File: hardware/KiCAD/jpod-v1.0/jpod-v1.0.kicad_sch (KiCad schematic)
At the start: 47 parts, among them J1 SD_Card, J2 SPI_DEBUG, J3 LCD_HEADER, J4 3.5mm Jack, Q1 AO3400A, U1 ESP32, U2 1.8V Regulator, U3 DAC, U4 Charger, U5 Buck Boost, U6 Fuel Gauge

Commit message: battery updates and switch added to library:
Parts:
- added S1: JS102011SAQN, JS102011SAQN:SW_JS102011SAQN, symbol jpod:JS102011SAQN
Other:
- note added: "These are for the AVDD/DVDD... power on DAC However they are identical. Maybe a cleaner way to display this?"
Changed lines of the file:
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@@
+    (effects (font (size 1.27 1.27)) (justify left bottom))
+  )
+  (text "These are for the AVDD/DVDD... power on DAC\nHowever they are identical. Maybe a cleaner way to display this?\n"
+    (at 18.288 159.512 0)
     (effects (font (size 1.27 1.27)) (justify left bottom))
   )
@@
         )
       )
+    )
+  )
+  (symbol (lib_id "jpod:JS102011SAQN") (at 519.049 279.781 0) (unit 1)
+    (in_bom yes) (on_board yes) (dnp no) (fields_autoplaced)
+    (property "Reference" "S1" (at 519.049 271.78 0)
+      (effects (font (size 1.27 1.27)))
+    )
+    (property "Value" "JS102011SAQN" (at 519.049 274.32 0)
+      (effects (font (size 1.27 1.27)))
+    )
+    (property "Footprint" "JS102011SAQN:SW_JS102011SAQN" (at 519.049 279.781 0)
+      (effects (font (size 1.27 1.27)) (justify bottom) hide)
+    )
+    (property "Datasheet" "" (at 519.049 279.781 0)
+      (effects (font (size 1.27 1.27)) hide)
+    )
+    (property "MANUFACTURER" "C&K" (at 519.049 279.781 0)
+      (effects (font (size 1.27 1.27)) (justify bottom) hide)
+    )
+    (pin "1")
+    (pin "2")
+    (pin "3")
+    (instances
+      (project "jpod-v1.0"
+        (path "/6f39d746-fc34-453f-ad9d-f86b2a09a03d"
+          (reference "S1") (unit 1)
+        )
+      )

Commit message: schematic work for charger completed
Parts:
- added C17, C18, C19: 4.7uF, Capacitor_SMD:C_0603_1608Metric, symbol Device:C
- added D1: APT1608SYCK, APT1608SYCK:LED_APT1608SYCK, symbol jpod:APT1608SYCK
- added D2: APT1608SGC, APT1608SGC:LED_APT1608SGC, symbol jpod:APT1608SGC
- added P1: BATTERY_CONN, jpod_footprints:S2B-PH-SM4-TB, symbol jpod:S2B-PH-SM4-TB
- added R16: 1.07K, Resistor_SMD:R_0603_1608Metric, symbol Device:R
- added R17: 887, Resistor_SMD:R_0603_1608Metric, symbol Device:R
- added R18: 46.4k, Resistor_SMD:R_0603_1608Metric, symbol Device:R
- added R19: 10K, Resistor_SMD:R_0603_1608Metric, symbol Device:R
- added R20, R21: 1K, Resistor_SMD:R_0603_1608Metric, symbol Device:R
- S1: value JS102011SAQN -> POWER_SWITCH
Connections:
- net GND: now also U4.15 (SYSOFF), U4.17 (EXP), U4.4 (~{CE}), U4.6 (EN1), U4.8 (VSS), C17.2, C18.2, C19.2, P1.2, R16.1, R17.2, R18.2, R19.2
- net at U4.1 (TS): now also R19.1
- net VSYS: now reaches U4.10 (OUT_10)
- net VSYS: now also U4.11 (OUT_11), U4.5 (EN2), C17.1, R20.1, R21.1
- net ILIM: now reaches U4.12 (ILIM)
- net ILIM: now also R16.2
- net VBUS: now reaches U4.13 (IN)
- net VBUS: now also C19.1
- net TMR: now reaches U4.14 (TMR)
- net TMR: now also R18.1
- net ISET: now reaches U4.16 (ISET)
- net ISET: now also R17.1
- net BAT: now reaches U4.2 (BAT_2)
- net BAT: now also U4.3 (BAT_3), C18.1, P1.1
- net PGOOD: now reaches U4.7 (~{PGOOD})
- net PGOOD: now also D2.1
- net CHG: now reaches U4.9 (~{CHG})
- net CHG: now also D1.1
- new net: D1.2, R21.2
- new net: D2.2, R20.2
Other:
- note added: "Charger output"
- note added: "Iset: 1A, K = 890 R = 887 Ichrg = K_Iset/R_Iset Ilim: 1.5A, k = 1610 R = 1.07K. Ilim = K/R"
- note added: "When layout PCB: Add no pin footprint for battery: 1528-1840-ND"
- moved on the sheet: S1, U4, U5, U6

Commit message: power sch finished
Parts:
- added C20, C21: 10uF, Capacitor_SMD:C_0603_1608Metric, symbol Device:C
- added C22: 100nF, Capacitor_SMD:C_0603_1608Metric, symbol Device:C
- added C23, C24, C25: 22uF, Capacitor_SMD:C_0603_1608Metric, symbol Device:C
- added C26: 0.1uF, Capacitor_SMD:C_0603_1608Metric, symbol Device:C
- added L1: 1.5uH, jpod_footprints:SRP4020TA-1R5M, symbol Device:L
- added R22: 1M, Resistor_SMD:R_0603_1608Metric, symbol Device:R
- added R23: 180K, Resistor_SMD:R_0603_1608Metric, symbol Device:R
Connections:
- net +3V3: now also U5.4 (VOUT_4), U5.5 (VOUT_5), C23.2, C24.2, C25.2, R22.2
- net BAT: now also U6.2 (CELL), U6.3 (VDD), C26.2
- net GND: now also S1.3, U5.15 (PGND), U5.2 (GND), U6.1 (CTG), U6.4 (GND), U6.6 (QSTRT), U6.9 (EP), C20.1, C21.1, C22.1, C23.1, C24.1, C25.1, C26.1, R23.1
- net SCL: now also U6.7 (SCL)
- net SDA: now also U6.8 (SDA)
- net VSYS: now also S1.1, U5.1 (VINA), U5.10 (VIN_10), U5.11 (VIN_11), U5.13 (PS/SYNC), C20.2, C21.2, C22.2
- net FUEL: now reaches U1.23 (IO15)
- net FUEL: now also U6.5 (~{ALERT})
- net BUCK_EN: now reaches U5.12 (EN)
- net BUCK_EN: now also S1.2
- net FB: now reaches U5.3 (FB)
- net FB: now also R22.1, R23.2
- net at U5.6 (L2_6): now also U5.7 (L2_7), L1.2
- net at U5.8 (L1_8): now also U5.9 (L1_9), L1.1
- no-connect marks 11 -> 12
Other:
- note added: "Charger input (USB - 5V)"
- moved on the sheet: C7, C8, S1, U2, U5, U6

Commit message: working on usb, vbus, and uart
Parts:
- added C27: 0.1uF, Capacitor_SMD:C_0603_1608Metric, symbol Device:C
- added J5: USB_CON, jpod:USB4105-GF-A, symbol jpod:USB4105-GF-A
- added R24, R25: 5.1K, Resistor_SMD:R_0603_1608Metric, symbol Device:R
- added R26: 22.1K, Resistor_SMD:R_0603_1608Metric, symbol Device:R
- added R27: 47.5K, Resistor_SMD:R_0603_1608Metric, symbol Device:R
- added U7: UART Bridge, jpod:CP2102N-A02-GQFN24R, symbol jpod:CP2102N-A02-GQFN24R
- added U8: ESD, jpod:USBLC6-2P6, symbol jpod:USBLC6-2P6
- U5: DESCRIPTION High Efficiency Single Inductor Buck-Boost Converter with 4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 -> (none)
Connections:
- net GND: now also C27.1, J5.A1_B12 (GND), J5.B1_A12 (GND__1), J5.SH1 (SHELL_GND), J5.SH2 (SHELL_GND__1), J5.SH3 (SHELL_GND__2), J5.SH4 (SHELL_GND__3), R24.2, R25.1, R27.1, U7.2 (GND), U7.25 (GND__1), U8.2 (GND)
- net VBUS: now also C27.2, J5.A4_B9 (VBUS), J5.B4_A9 (VBUS__1), R26.2, U8.5 (VBUS)
- net RX: now reaches U1.34 (RXD0)
- net RX: now also U7.21 (TXD)
- net TX: now reaches U1.35 (TXD0)
- net TX: now also U7.20 (RXD)
- new net: J5.A5 (CC1), R24.1
- new net: J5.B5 (CC2), R25.2
- new net D+: U8.6 (I/01)
- new net D-: U8.4 (I/02)
- new net DN: J5.A7 (DN1), J5.B7 (DN2), U8.3 (I/02)
- new net DP: J5.A6 (DP1), J5.B6 (DP2), U8.1 (I/01)
- new net I/01: U7.3 (D+)
- new net I/02: U7.4 (D-)
- new net VBUS_OUT: R26.1, R27.2, U7.8 (VBUS)
- no-connect marks 12 -> 14
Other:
- note added: "References from ESP RX to UART TX"
- note added: "References from ESP TX to UART RX"
- moved on the sheet: C1, C10, C11, C12, C13, C14, C15, C16, C17, C18, C19, C2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

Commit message: working mainly on the uart bridge
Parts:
- added C28: 4.7uF, Capacitor_SMD:C_0603_1608Metric, symbol Device:C
- added C29: 0.1uF, Capacitor_SMD:C_0603_1608Metric, symbol Device:C
- added R28: 1K, Resistor_SMD:R_0603_1608Metric, symbol Device:R
- U2: value 1.8V Regulator -> 1.8V_Regulator
- U5: value Buck Boost -> Buck_Boost
- U6: value Fuel Gauge -> Fuel_Gauge
- U7: value UART Bridge -> UART_Bridge
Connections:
- net +3V3: now also U7.6 (VDD), C28.2, C29.2
- net GND: now also C28.1, C29.1
- net RX: no longer U7.21 (TXD)
- net TX: no longer U7.20 (RXD)
- net VBUS: now also U7.7 (VREGIN)
- net at U7.5 (VIO): now also R28.1
- net at U7.9 (~{RST}): now also R28.2
- new net ESP_RXD0: U7.21 (TXD)
- new net ESP_TXD0: U7.20 (RXD)
- no-connect marks 14 -> 24

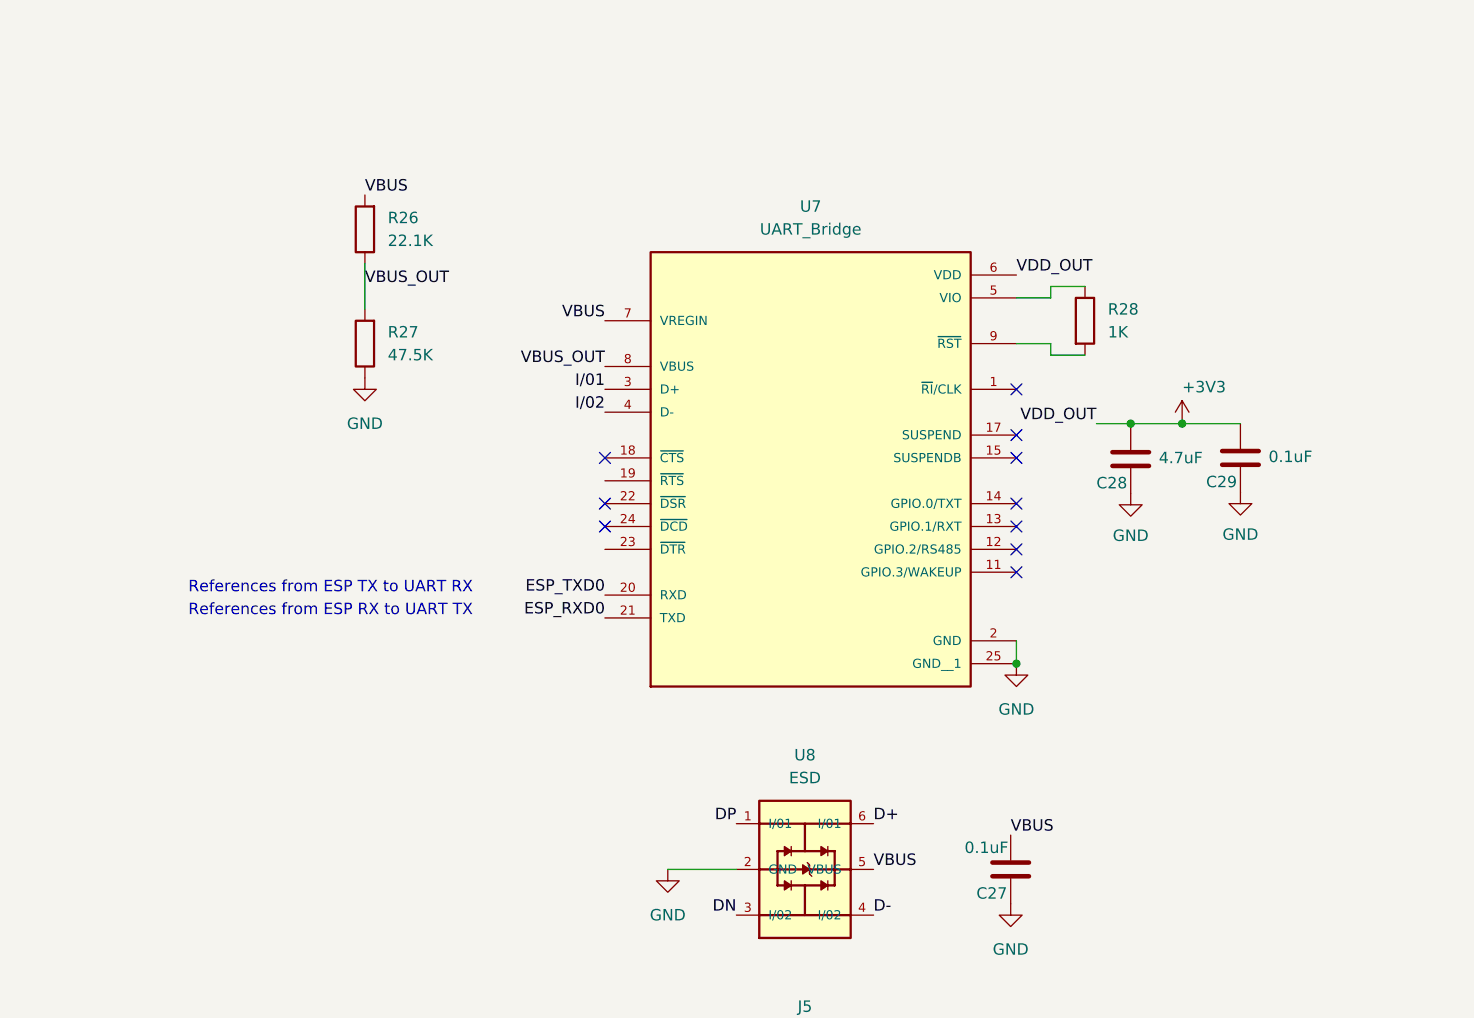
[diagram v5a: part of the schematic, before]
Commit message: swtich UART bridge to be self-powered, along with fixing RTSb and DTRb's communication with ESP
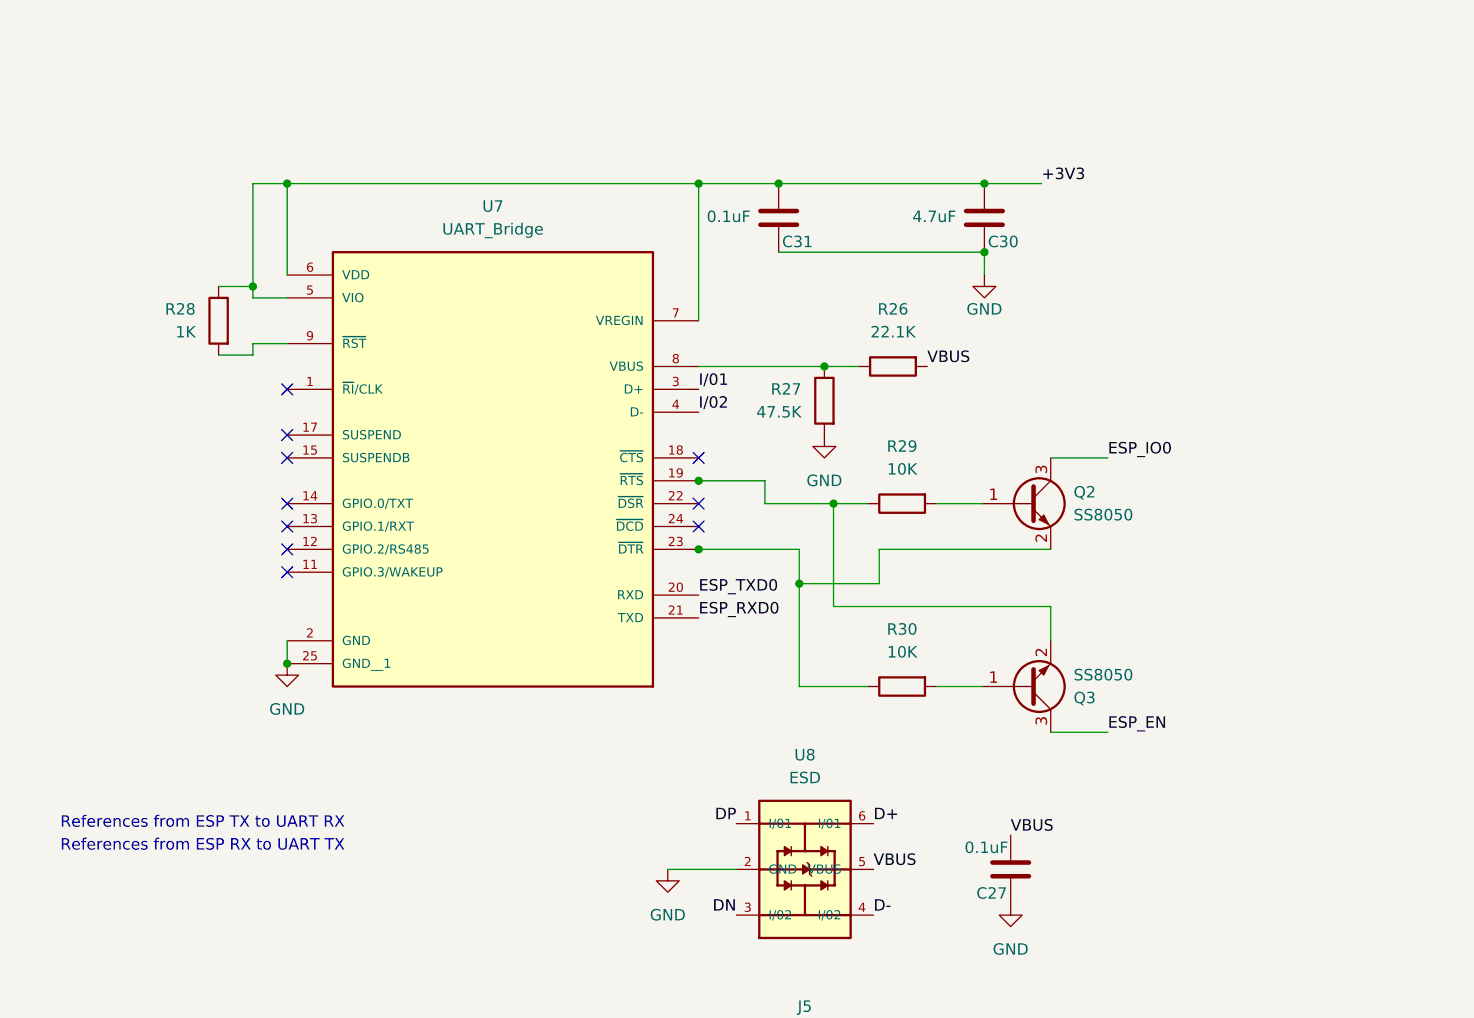
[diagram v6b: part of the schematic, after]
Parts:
- removed C28: 4.7uF, Capacitor_SMD:C_0603_1608Metric, symbol Device:C
- removed C29: 0.1uF, Capacitor_SMD:C_0603_1608Metric, symbol Device:C
- added C30: 4.7uF, Capacitor_SMD:C_0603_1608Metric, symbol Device:C
- added C31: 0.1uF, Capacitor_SMD:C_0603_1608Metric, symbol Device:C
- added Q2, Q3: SS8050, Package_TO_SOT_SMD:SOT-23, symbol Transistor_BJT:SS8050
- added R29, R30: 10K, Resistor_SMD:R_0603_1608Metric, symbol Device:R
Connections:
- net +3V3: now also R28.1, U7.5 (VIO), U7.7 (VREGIN), C30.2, C31.2
- net GND: now also R27.2, C30.1, C31.1; no longer R27.1
- net VBUS: no longer U7.7 (VREGIN)
- net at U7.19 (~{RTS}): now also Q3.2 (E), R29.1
- net at U7.23 (~{DTR}): now also Q2.2 (E), R30.1
- net VBUS_OUT: no longer names the net of R26.1, U7.8 (VBUS)
- net VBUS_OUT: now also R27.1; no longer R27.2
- new net: Q3.1 (B), R30.2
- new net: Q2.1 (B), R29.2
- new net ESP_EN: Q3.3 (C)
- new net ESP_IO0: Q2.3 (C)
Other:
- moved on the sheet: R28, U7

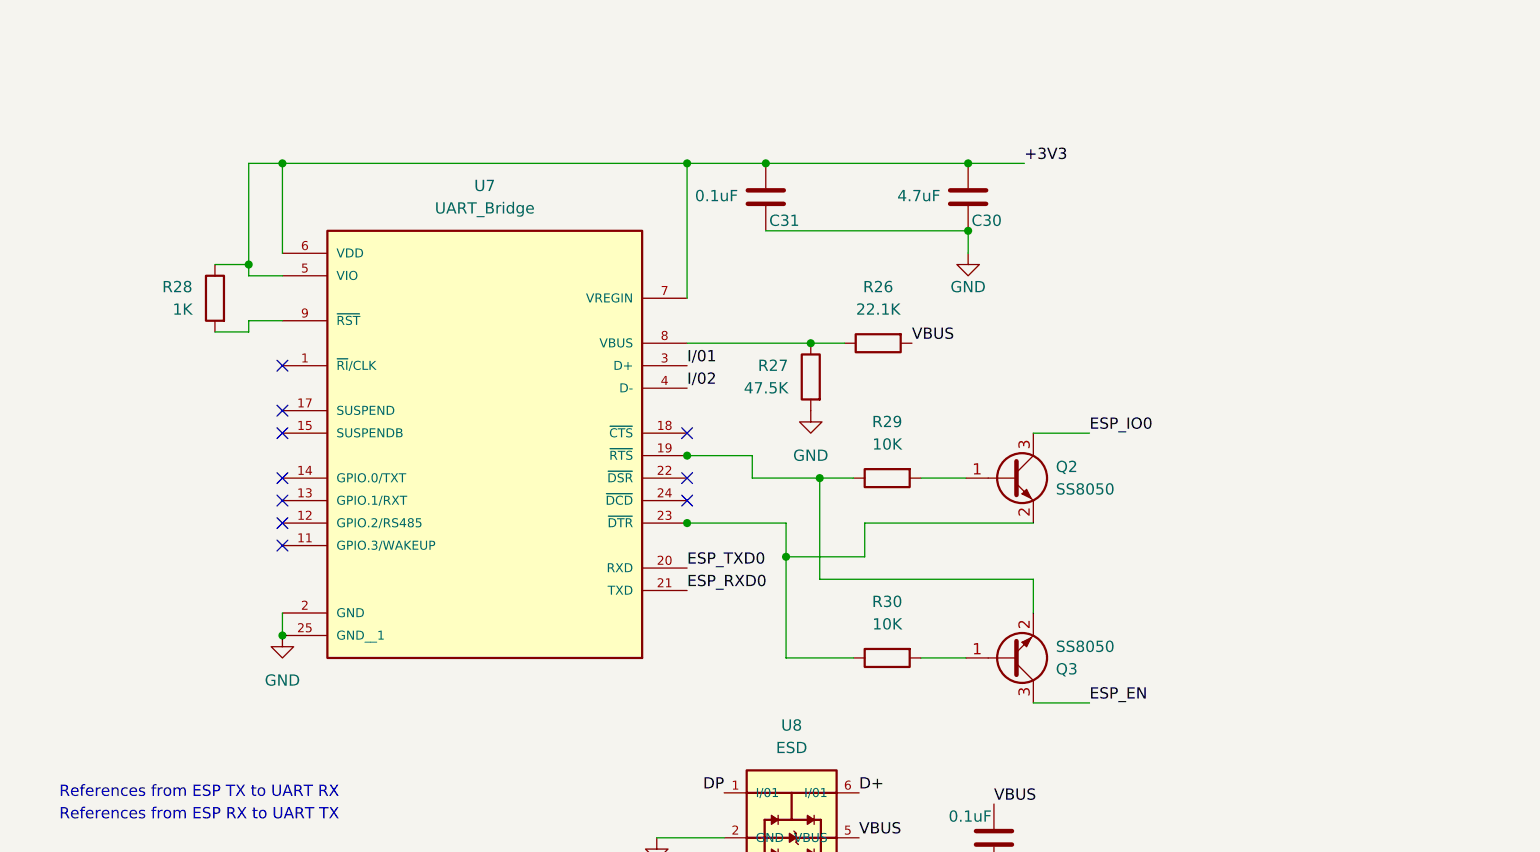
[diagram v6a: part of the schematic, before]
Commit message: added transistor model and made changes to the en and io0 esp traces
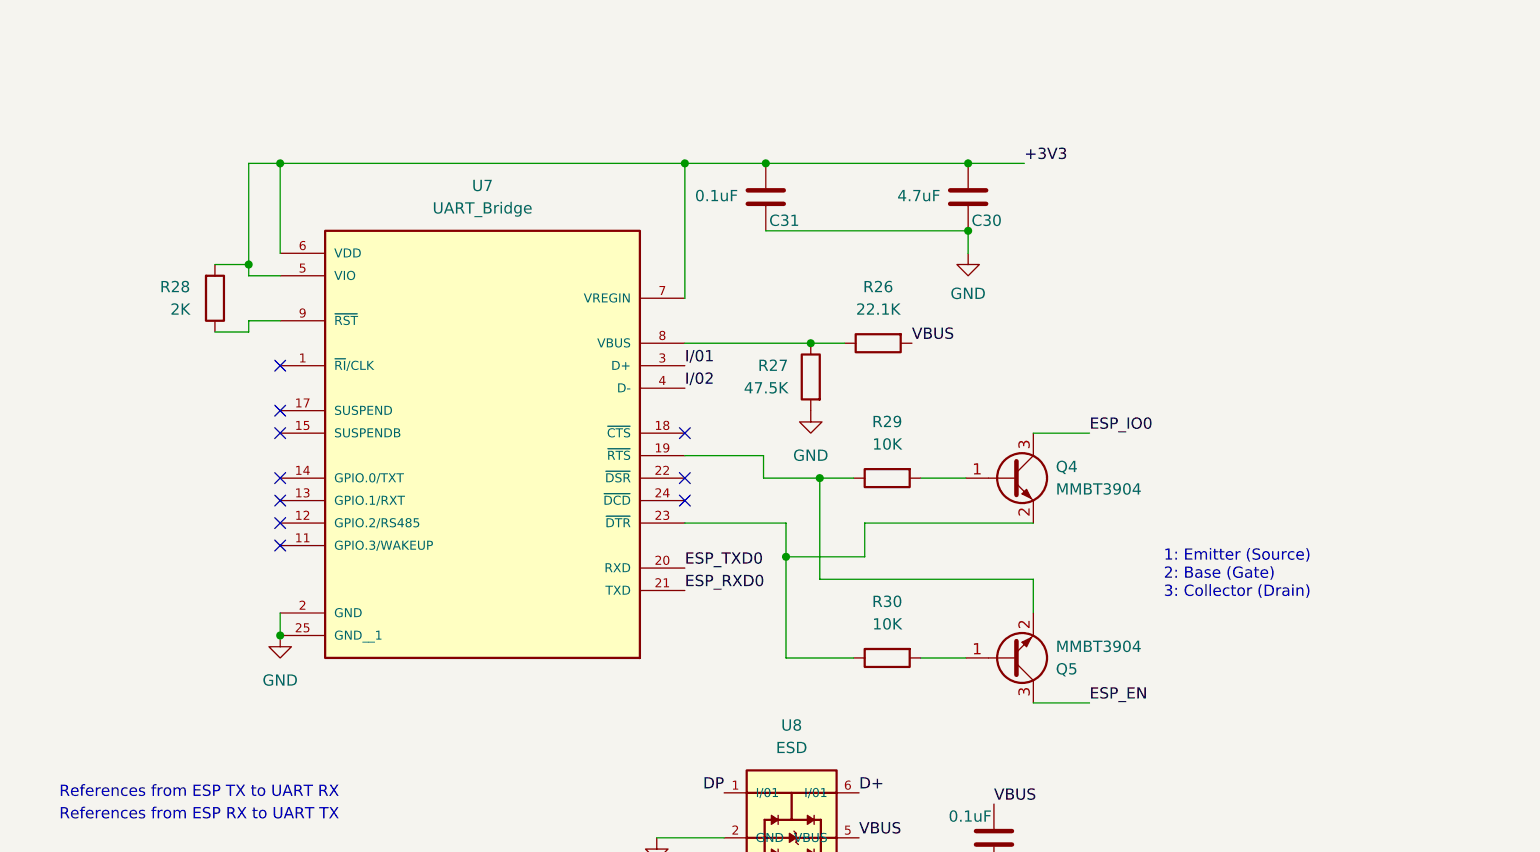
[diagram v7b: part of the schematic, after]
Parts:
- removed Q2, Q3: SS8050, Package_TO_SOT_SMD:SOT-23, symbol Transistor_BJT:SS8050
- added Q4, Q5: MMBT3904, Package_TO_SOT_SMD:SOT-23, symbol Transistor_BJT:MMBT3904
- R28: value 1K -> 2K
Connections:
- net +3V3: now also R28.2; no longer R28.1
- net ESP_EN: now also Q5.3 (C)
- net ESP_IO0: now also Q4.3 (C)
- net at R30.1, U7.23 (~{DTR}): now also Q4.2 (E)
- net at R30.2: now also Q5.1 (B)
- net at R29.2: now also Q4.1 (B)
- net at R29.1, U7.19 (~{RTS}): now also Q5.2 (E)
- net at U7.9 (~{RST}): now also R28.1; no longer R28.2
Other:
- note added: "1: Emitter (Source) 2: Base (Gate) 3: Collector (Drain)"
